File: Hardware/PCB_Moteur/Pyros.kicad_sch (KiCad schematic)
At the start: 33 parts, among them J17 Screw_Terminal_01x04, Q1 SI5442DU-T1-GE3, Q2 SI5442DU-T1-GE3, Q3 MMBT3904, Q4 SI7617DN-T1-GE3, U6 LM393

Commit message: wip: GND vias et power polygon  patching
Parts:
- Q1, Q2: footprint pcb_moteur:SI5442DU_T1_G3 -> SON_8DU-T1-GE3_VIS
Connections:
- net Pyro1-: now also Q1.6 (D); no longer Q1.1 (D)
- net Pyro2-: now also Q2.6 (D); no longer Q2.1 (D)
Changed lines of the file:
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@@
 			)
 		)
-		(property "Footprint" "pcb_moteur:SI5442DU_T1_G3"
+		(property "Footprint" "SON_8DU-T1-GE3_VIS"
 			(at 113.03 133.096 0)
 			(effects
@@
 		)
 		(pin "4"
+		)
+		(pin "7"
+		)
+		(pin "3"
+		)
+		(pin "6"
+		)
+		(pin "9"
+		)
+		(pin "8"
+		)
+		(pin "2"
 		)
 		(instances
@@
 			)
 		)
-		(property "Footprint" "pcb_moteur:SI5442DU_T1_G3"
+		(property "Footprint" "SON_8DU-T1-GE3_VIS"
 			(at 44.45 133.096 0)
 			(effects
@@
 		(pin "4"
 		)
-		(instances
+		(pin "7"
+		)
+		(pin "9"
+		)
+		(pin "8"
+		)
+		(pin "2"
+		)
+		(pin "3"
+		)
+		(pin "6"
+		)
+		(instances

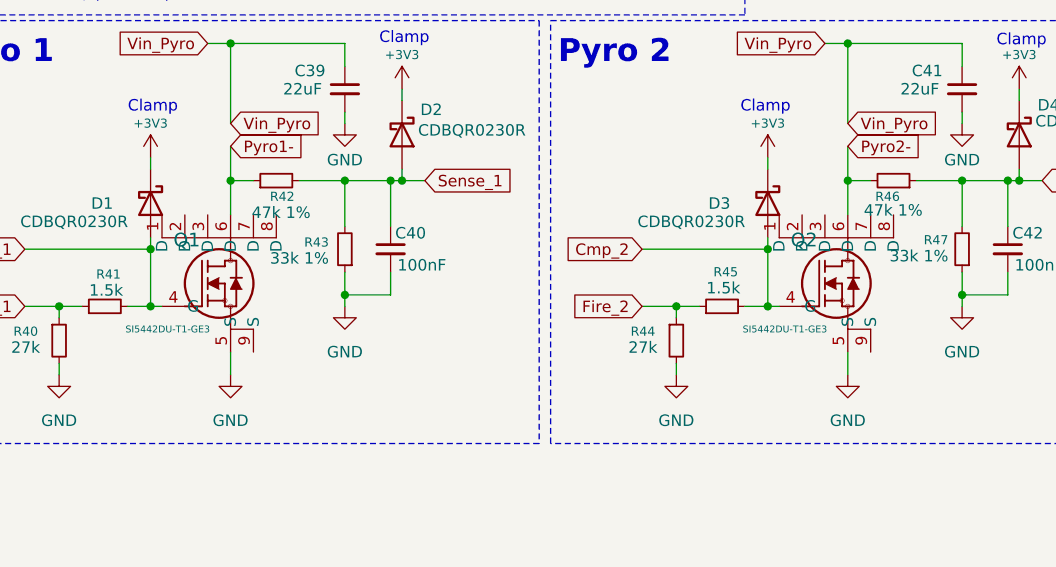
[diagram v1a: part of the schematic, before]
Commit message: feat(moteur): add 8MHz crystal (only schematic), fix ERC, update stm32 project, remove extend ios
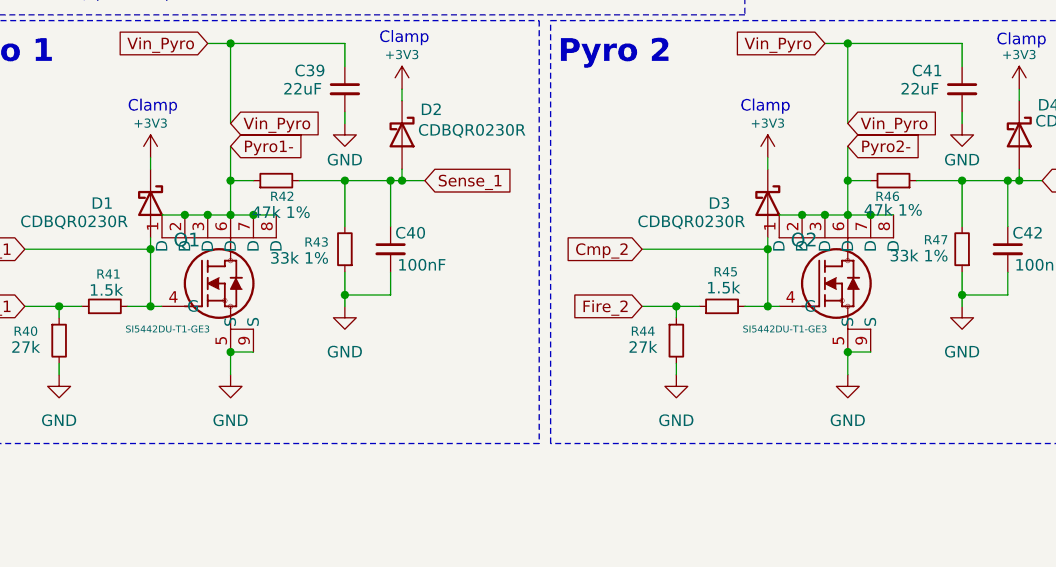
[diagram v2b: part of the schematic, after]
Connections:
- net GND: now also Q1.9 (S), Q2.9 (S)
- net Pyro1-: now also Q1.1 (D), Q1.2 (D), Q1.3 (D), Q1.7 (D), Q1.8 (D)
- net Pyro2-: now also Q2.1 (D), Q2.2 (D), Q2.3 (D), Q2.7 (D), Q2.8 (D)
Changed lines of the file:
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@@
+	)
+	(junction
+		(at 46.99 120.65)
+		(diameter 0)
+		(color 0 0 0 0)
 	)
 	(junction
@@
 	)
 	(junction
+		(at 46.99 105.41)
+		(diameter 0)
+		(color 0 0 0 0)
+	)
+	(junction
 		(at 266.7 33.02)
 		(diameter 0)
@@
 	)
 	(junction
+		(at 113.03 105.41)
+		(diameter 0)
+		(color 0 0 0 0)
+	)
+	(junction
 		(at 85.09 54.61)
 		(diameter 0)
@@
 	)
 	(junction
+		(at 110.49 105.41)
+		(diameter 0)
+		(color 0 0 0 0)
+	)
+	(junction
 		(at 133.35 101.6)
 		(diameter 0)
@@
 	)
 	(junction
+		(at 118.11 105.41)
+		(diameter 0)
+		(color 0 0 0 0)
+	)
+	(junction
+		(at 44.45 105.41)
+		(diameter 0)
+		(color 0 0 0 0)
+	)
+	(junction
 		(at 38.1 109.22)
 		(diameter 0)
@@
 	)
 	(junction
+		(at 115.57 105.41)
+		(diameter 0)
+		(color 0 0 0 0)
+	)
+	(junction
+		(at 49.53 105.41)
+		(diameter 0)
+		(color 0 0 0 0)
+	)
+	(junction
 		(at 115.57 86.36)
 		(diameter 0)
@@
 	)
 	(junction
+		(at 41.91 105.41)
+		(diameter 0)
+		(color 0 0 0 0)
+	)
+	(junction
 		(at 223.52 35.56)
 		(diameter 0)
@@
 	)
 	(junction
+		(at 115.57 120.65)
+		(diameter 0)
+		(color 0 0 0 0)
+	)
+	(junction
 		(at 38.1 115.57)
 		(diameter 0)
@@
 	(wire
 		(pts
+			(xy 115.57 105.41) (xy 118.11 105.41)
+		)
+		(stroke
+			(width 0)
+			(type default)
+		)
+	)
+	(wire
+		(pts
 			(xy 38.1 115.57) (xy 39.37 115.57)
 		)
@@
 	(wire
 		(pts
+			(xy 39.37 105.41) (xy 41.91 105.41)
+		)
+		(stroke
+			(width 0)
+			(type default)
+		)
+	)
+	(wire
+		(pts
 			(xy 104.14 115.57) (xy 106.68 115.57)
 		)
@@
 	(wire
 		(pts
+			(xy 41.91 105.41) (xy 44.45 105.41)
+		)
+		(stroke
+			(width 0)
+			(type default)
+		)
+	)
+	(wire
+		(pts
 			(xy 204.47 60.96) (xy 204.47 62.23)
 		)
@@
 	(wire
 		(pts
+			(xy 107.95 105.41) (xy 110.49 105.41)
+		)
+		(stroke
+			(width 0)
+			(type default)
+		)
+	)
+	(wire
+		(pts
 			(xy 128.27 86.36) (xy 128.27 88.9)
 		)
@@
 	(wire
 		(pts
+			(xy 115.57 120.65) (xy 118.11 120.65)
+		)
+		(stroke
+			(width 0)
+			(type default)
+		)
+	)
+	(wire
+		(pts
 			(xy 134.62 100.33) (xy 134.62 101.6)
 		)
@@
 	(wire
 		(pts
+			(xy 44.45 105.41) (xy 46.99 105.41)
+		)
+		(stroke
+			(width 0)
+			(type default)
+		)
+	)
+	(wire
+		(pts
 			(xy 217.17 27.94) (xy 223.52 27.94)
 		)
@@
 	(wire
 		(pts
+			(xy 46.99 105.41) (xy 49.53 105.41)
+		)
+		(stroke
+			(width 0)
+			(type default)
+		)
+	)
+	(wire
+		(pts
 			(xy 115.57 86.36) (xy 115.57 95.25)
 		)
@@
 	(wire
 		(pts
+			(xy 113.03 105.41) (xy 115.57 105.41)
+		)
+		(stroke
+			(width 0)
+			(type default)
+		)
+	)
+	(wire
+		(pts
 			(xy 265.43 54.61) (xy 266.7 54.61)
 		)
@@
 	(wire
 		(pts
+			(xy 46.99 120.65) (xy 49.53 120.65)
+		)
+		(stroke
+			(width 0)
+			(type default)
+		)
+	)
+	(wire
+		(pts
 			(xy 223.52 25.4) (xy 223.52 27.94)
 		)
@@
 	(wire
 		(pts
+			(xy 49.53 105.41) (xy 52.07 105.41)
+		)
+		(stroke
+			(width 0)
+			(type default)
+		)
+	)
+	(wire
+		(pts
 			(xy 24.13 109.22) (xy 38.1 109.22)
 		)
@@
 	(wire
 		(pts
+			(xy 118.11 105.41) (xy 120.65 105.41)
+		)
+		(stroke
+			(width 0)
+			(type default)
+		)
+	)
+	(wire
+		(pts
 			(xy 26.67 43.18) (xy 26.67 48.26)
 		)
@@
 		)
 		(stroke
+			(width 0)
+			(type default)
+		)
+	)
+	(wire
+		(pts
+			(xy 110.49 105.41) (xy 113.03 105.41)
+		)
+		(stroke

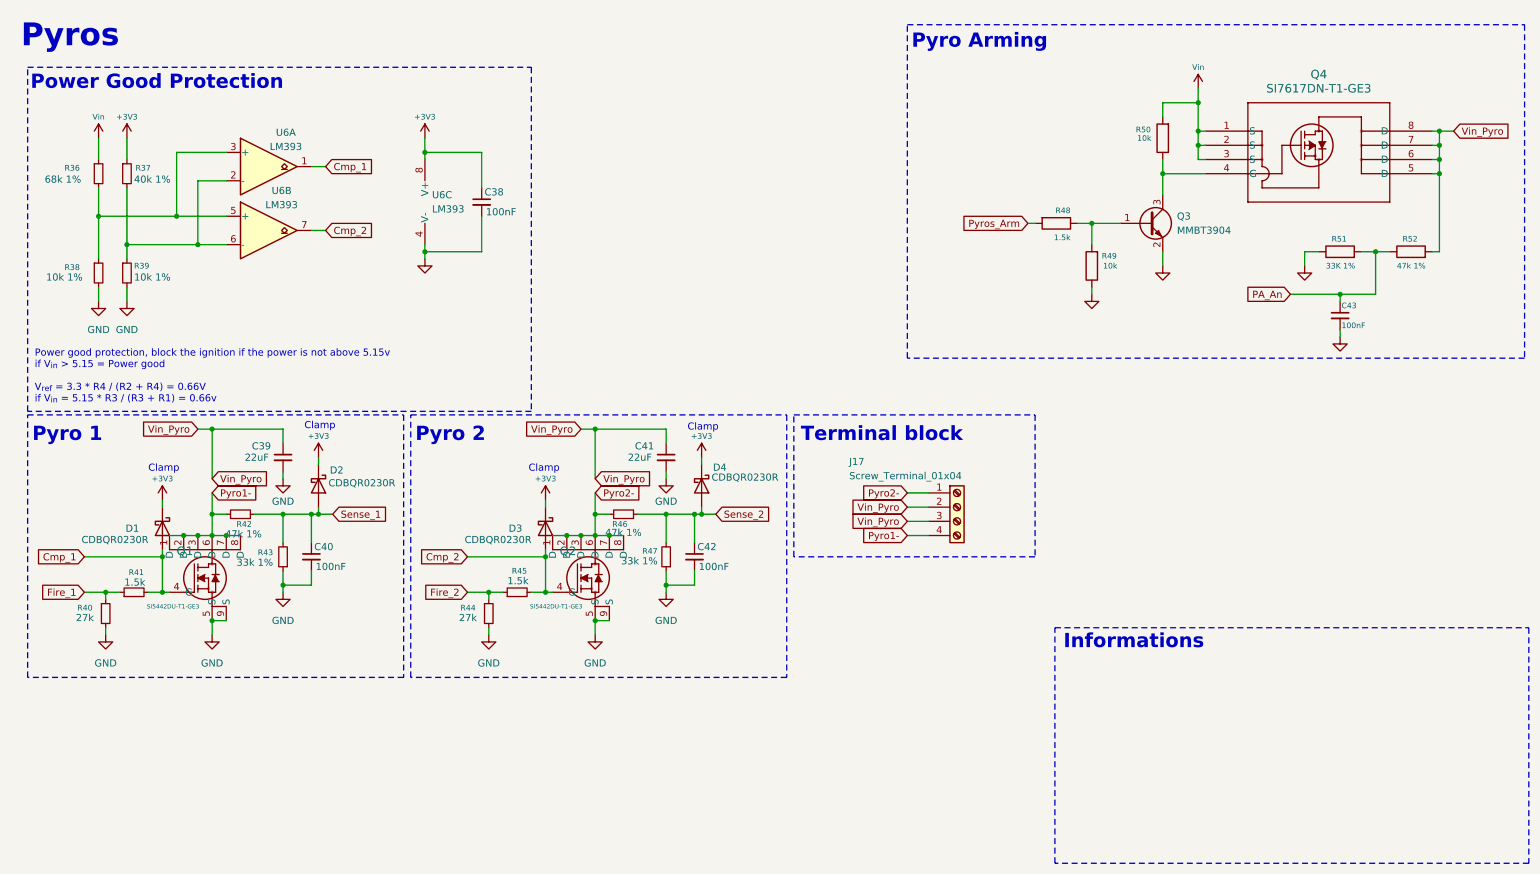
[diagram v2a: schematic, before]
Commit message: fix(GSE & Moteur): change Vin adc divider
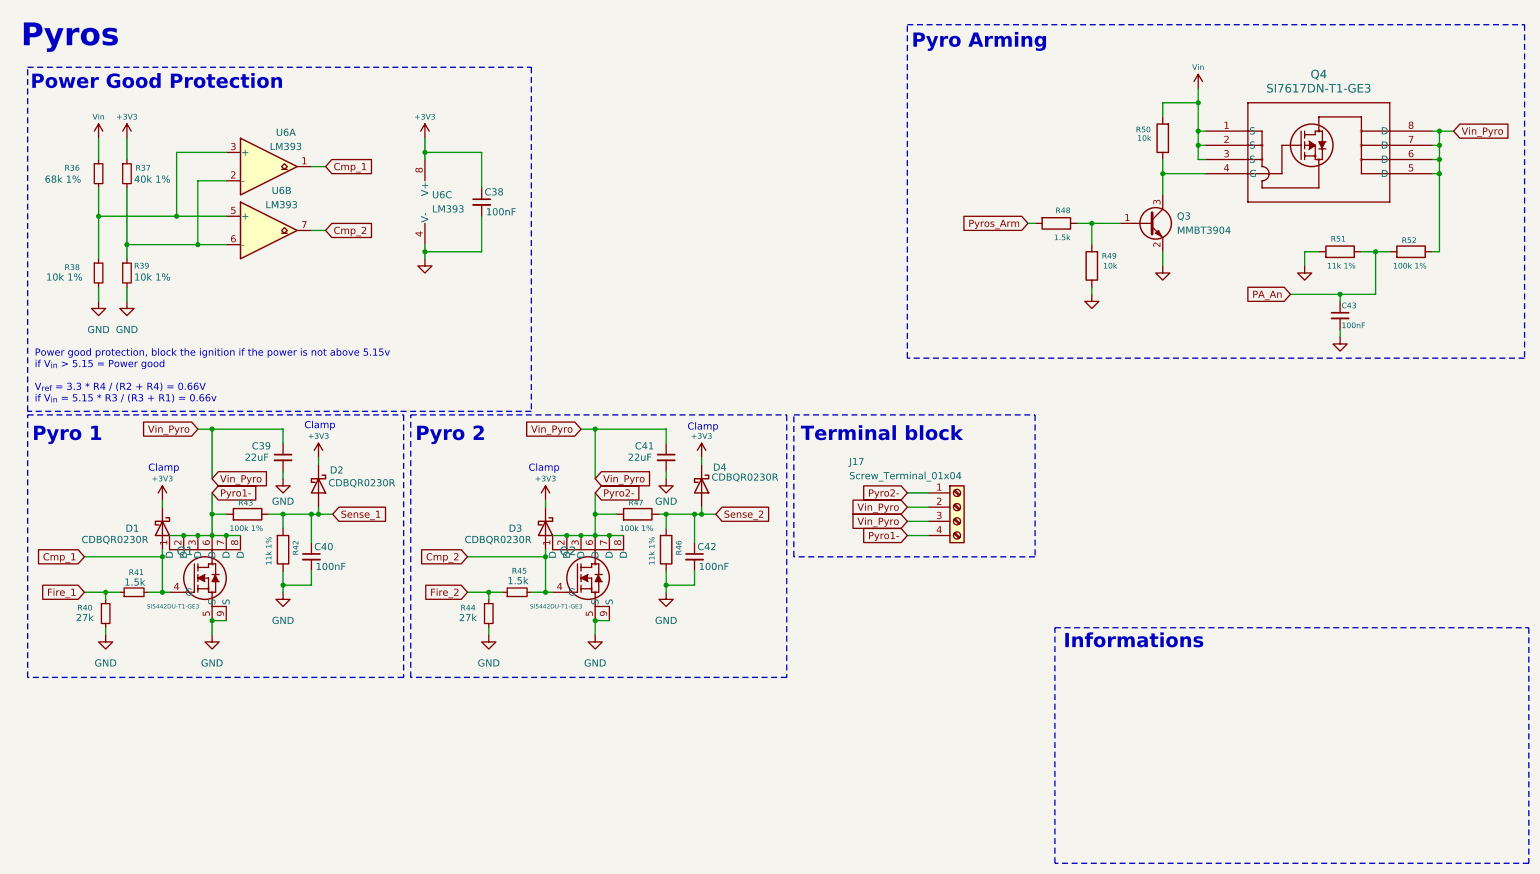
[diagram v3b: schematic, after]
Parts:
- removed R42, R46: 47k 1%, Resistor_SMD:R_0805_2012Metric, symbol Device:R_Small
- removed R43, R47: 33k 1%, Resistor_SMD:R_0805_2012Metric, symbol Device:R_Small
- added R42, R46: 11k 1%, Resistor_SMD:R_0805_2012Metric, symbol Device:R
- added R43, R47: 100k 1%, Resistor_SMD:R_0805_2012Metric, symbol Device:R
- R51: value 33K 1% -> 11k 1%
- R52: value 47k 1% -> 100k 1%
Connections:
- net GND: now also R51.2, R42.1, R46.1; no longer R51.1
- net PA_An: now also R51.1, R52.2; no longer R51.2, R52.1
- net Pyro1-: now also R43.2
- net Pyro2-: now also R47.2
- net Sense_1: now also R42.2, R43.1
- net Sense_2: now also R46.2, R47.1
- net Vin_Pyro: now also R52.1; no longer R52.2

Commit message: wip : work on silkscreen and add all info to BOM
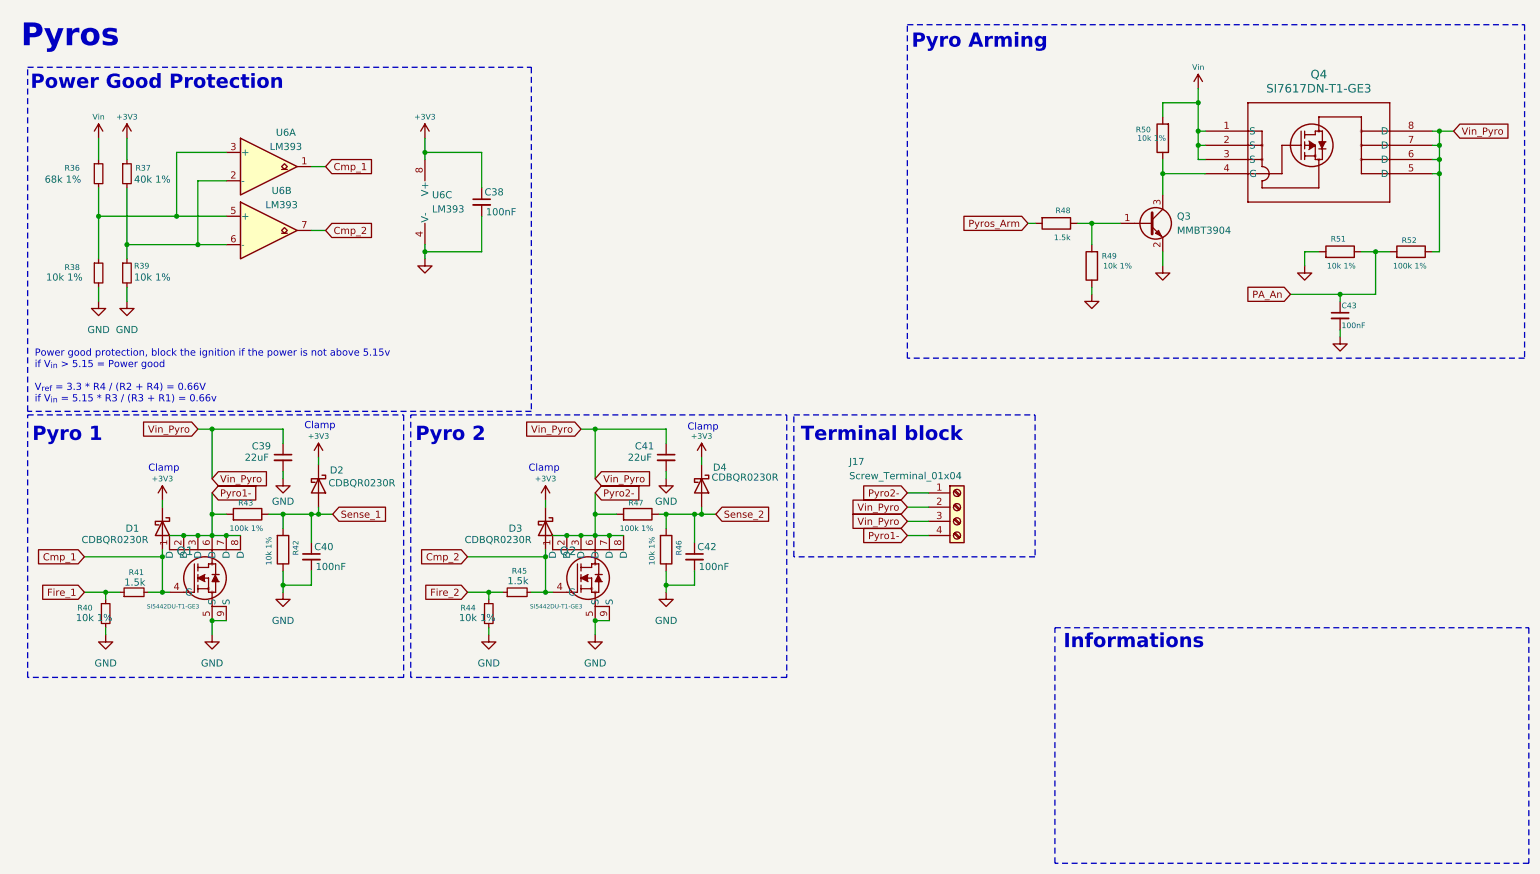
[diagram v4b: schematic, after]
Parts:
- C38, C40, C42, C43: DigiKey_Part_Number (none) -> 399-C0805C104K5RACTUCT-ND; Manufacturer_Part_Number (none) -> C0805C104K5RACTU
- C39, C41: DigiKey_Part_Number (none) -> 445-14428-1-ND; Manufacturer_Part_Number (none) -> C2012X5R1V226M125AC
- D1, D2, D3, D4: footprint Diode_SMD:D_SOD-923 -> Diode_SMD:D_0603_1608Metric; DigiKey_Part_Number (none) -> CD0603-B0340RCT-ND; Manufacturer_Part_Number (none) -> CD0603-B0340R
- J17: DigiKey_Part_Number (none) -> ED10563-ND; Manufacturer_Part_Number (none) -> OSTVN04A150
- Q1, Q2: DigiKey_Part_Number (none) -> SI5442DU-T1-GE3CT-ND; Manufacturer_Part_Number (none) -> SI5442DU-T1-GE3
- Q3: DigiKey_Part_Number (none) -> MMBT3904LT1GOSCT-ND; Manufacturer_Part_Number (none) -> MMBT3904LT1G
- Q4: DigiKey_Part_Number (none) -> SI7617DN-T1-GE3CT-ND; Manufacturer_Part_Number (none) -> SI7617DN-T1-GE3
- R36: DigiKey_Part_Number (none) -> RMCF0805FT68K0CT-ND; Manufacturer_Part_Number (none) -> RMCF0805FT68K0
- R37: DigiKey_Part_Number (none) -> 541-CRCW080540K0FKEACT-ND; Manufacturer_Part_Number (none) -> CRCW080540K0FKEA
- R38, R39: DigiKey_Part_Number (none) -> 541-10.0KCCT-ND; Manufacturer_Part_Number (none) -> CRCW080510K0FKEA
- R40, R44: value 27k -> 10k 1%; DigiKey_Part_Number (none) -> 541-10.0KCCT-ND; Manufacturer_Part_Number (none) -> CRCW080510K0FKEA
- R41, R45, R48: DigiKey_Part_Number (none) -> P1.5KDBCT-ND; Manufacturer_Part_Number (none) -> ERA-3AEB152V
- R42, R46, R51: value 11k 1% -> 10k 1%; DigiKey_Part_Number (none) -> 541-10.0KCCT-ND; Manufacturer_Part_Number (none) -> CRCW080510K0FKEA
- R43, R47, R52: DigiKey_Part_Number (none) -> 311-100KCRCT-ND; Manufacturer_Part_Number (none) -> RC0805FR-07100KL
- R49, R50: value 10k -> 10k 1%; DigiKey_Part_Number (none) -> 541-10.0KCCT-ND; Manufacturer_Part_Number (none) -> CRCW080510K0FKEA
- U6: DigiKey_Part_Number (none) -> 296-1015-1-ND; Manufacturer_Part_Number (none) -> LM393DR

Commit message: wip : reorder refdes and fix footprints
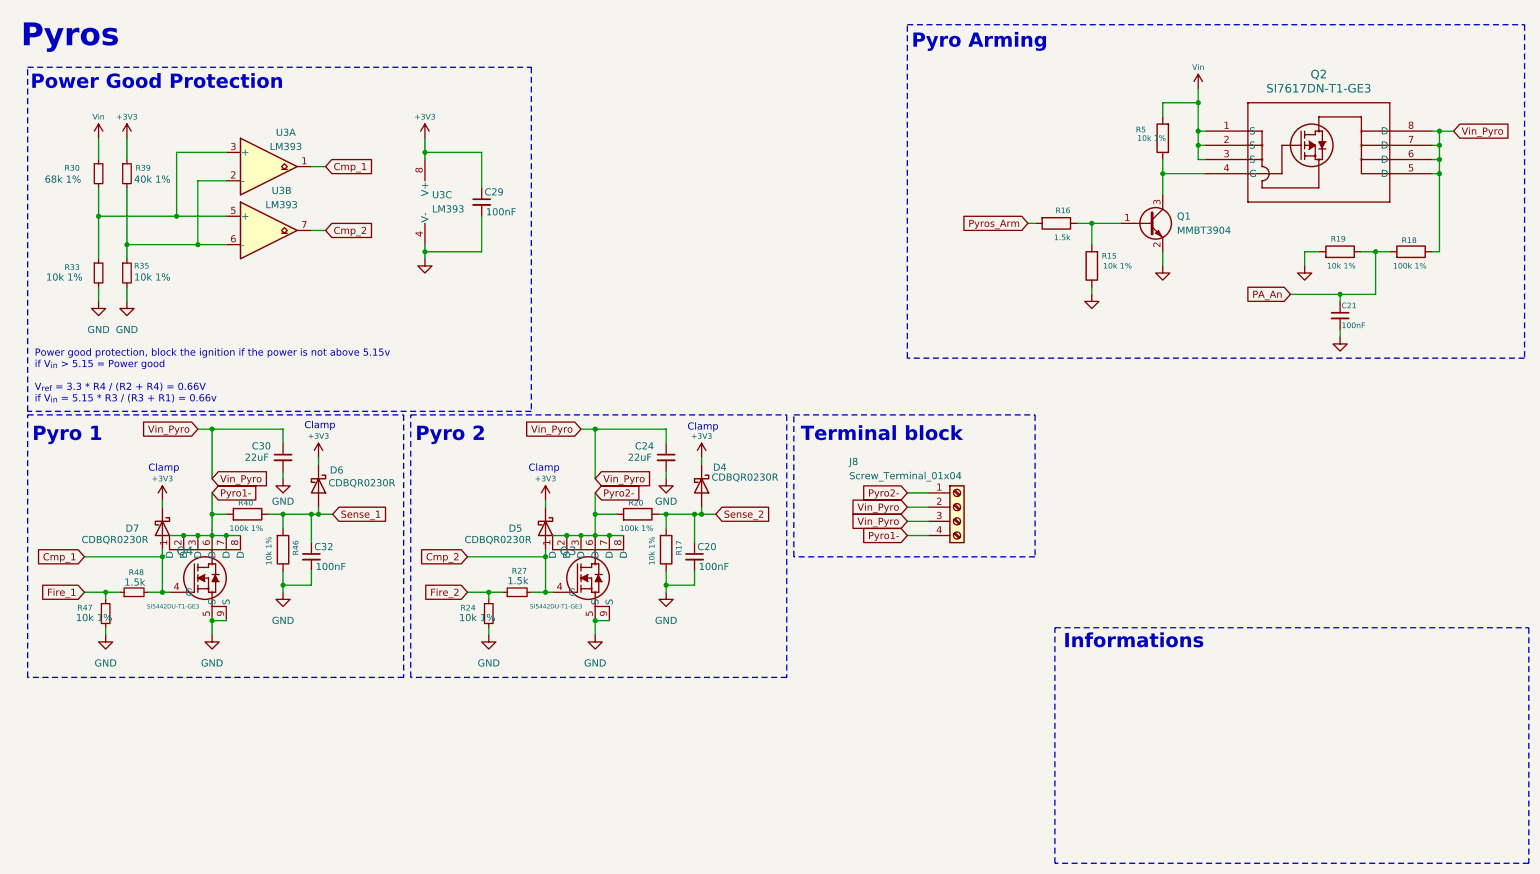
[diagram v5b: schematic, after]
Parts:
- Q3: renamed from Q2; footprint SON_8DU-T1-GE3_VIS -> pcb_moteur:SON_8DU-T1-GE3_VIS
- Q4: renamed from Q1; footprint SON_8DU-T1-GE3_VIS -> pcb_moteur:SON_8DU-T1-GE3_VIS
- renumbered C42 to C20, C43 to C21, C41 to C24, C38 to C29, C39 to C30, C40 to C32, D3 to D5, D2 to D6, D1 to D7, J17 to J8, Q3 to Q1, Q4 to Q2, R49 to R15, R48 to R16, R46 to R17, R52 to R18, R51 to R19, R47 to R20, R44 to R24, R45 to R27, R36 to R30, R38 to R33, R39 to R35, R37 to R39, R43 to R40, R42 to R46, R40 to R47, R41 to R48, R50 to R5, U6 to U3
